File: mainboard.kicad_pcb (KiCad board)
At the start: 2 copper layers, 67.3 x 33.7 mm, 29 parts, among them J1 105017-1001, J2 Conn_01x04_Female, J3 Conn_01x02_Female, J5 Conn_01x02_Female, Q1 AOD4184A, U1 ESP32-WROOM-32E_(16MB), U3 AMS1117-3.3, U4 PAM8403DR

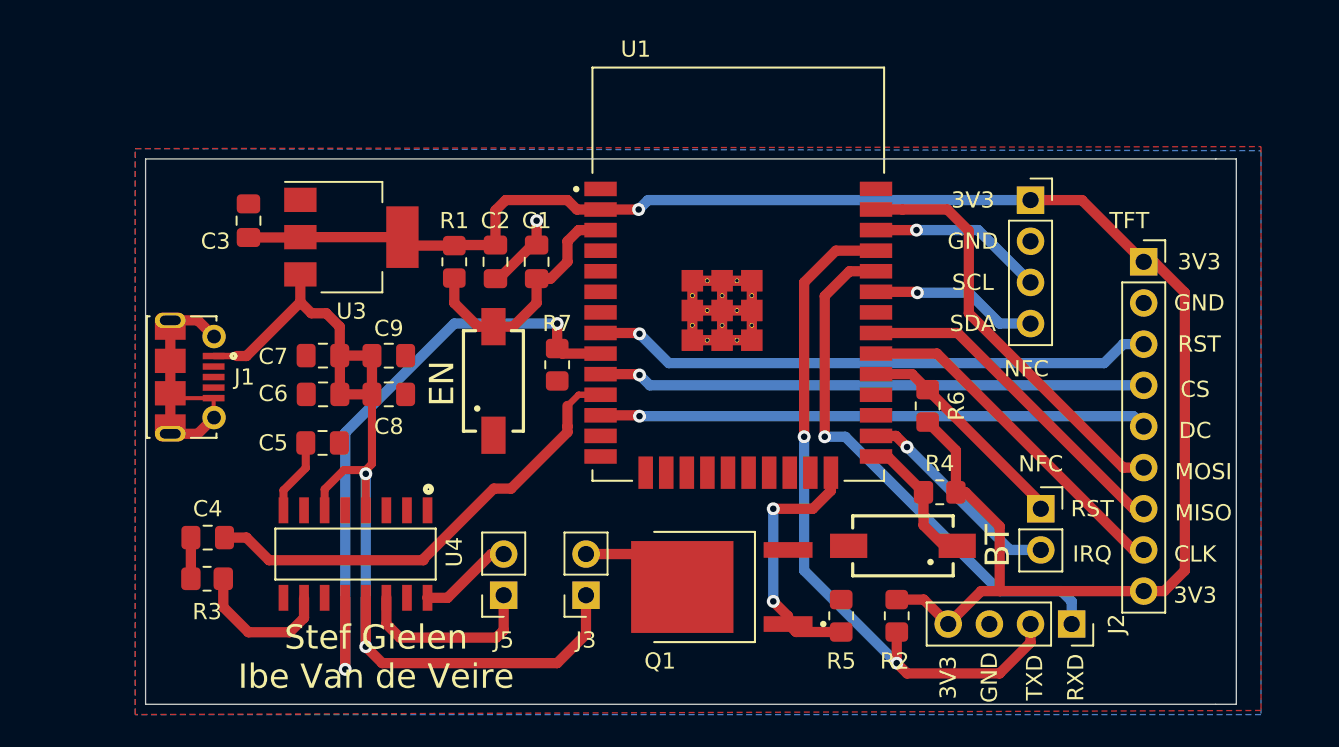
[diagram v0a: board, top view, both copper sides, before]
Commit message: update volgens feedback
blinkled toegevoegd aan io12
paar grondvias toegevoegd
ingangsontkoppeling ldo
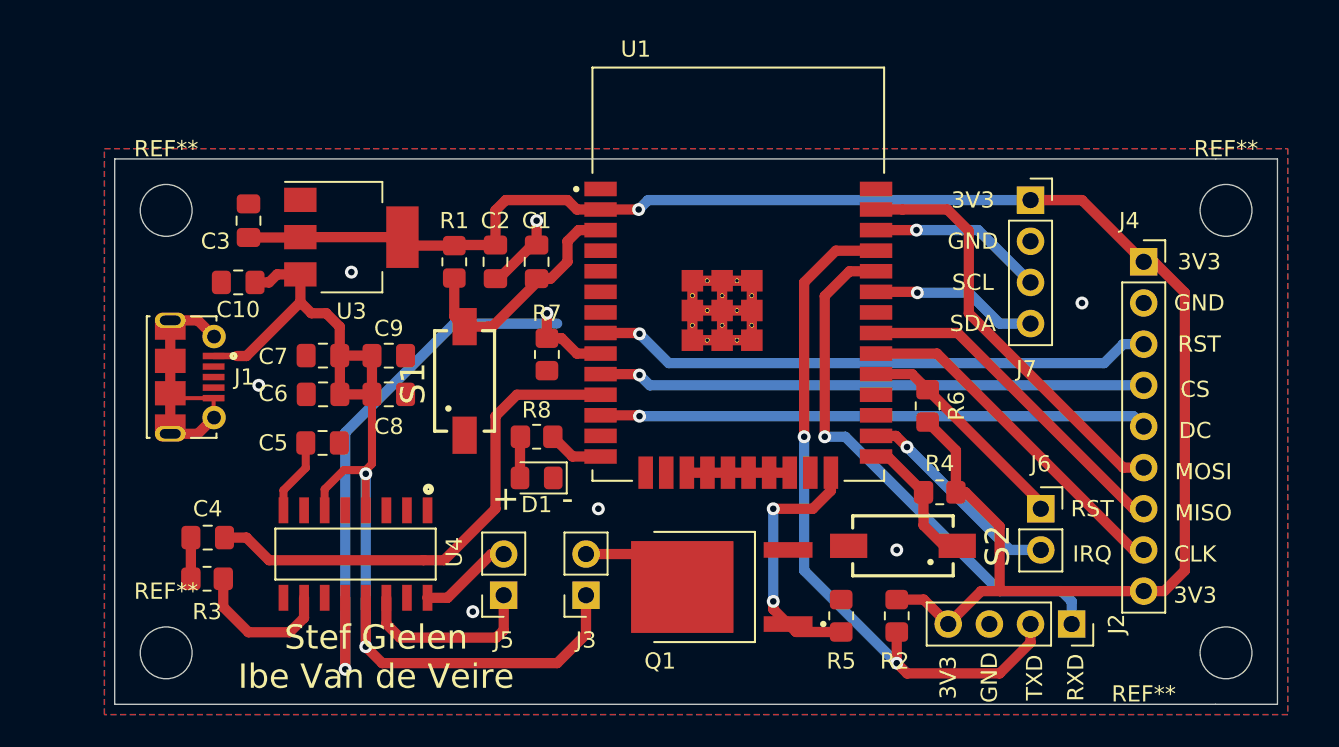
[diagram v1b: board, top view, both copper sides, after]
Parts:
- added C10: 10u, Capacitor_SMD:C_0805_2012Metric_Pad1.18x1.45mm_HandSolder, F.Cu at (83.2, 90.2)
- added D1: LED, LED_SMD:LED_0805_2012Metric_Pad1.15x1.40mm_HandSolder, F.Cu at (101.6, 102.2)
- added R8: 47???, Resistor_SMD:R_0805_2012Metric_Pad1.20x1.40mm_HandSolder, F.Cu at (101.6, 99.7)
- added REF**: MountingHole_3.2mm_M3_DIN965, MountingHole:MountingHole_3.2mm_M3_DIN965, F.Cu at (144.1, 85.7)
- added REF**: MountingHole_3.2mm_M3_DIN965, MountingHole:MountingHole_3.2mm_M3_DIN965, F.Cu at (144.1, 113.0)
- added REF**: MountingHole_3.2mm_M3_DIN965, MountingHole:MountingHole_3.2mm_M3_DIN965, F.Cu at (78.7, 85.7)
- added REF**: MountingHole_3.2mm_M3_DIN965, MountingHole:MountingHole_3.2mm_M3_DIN965, F.Cu at (78.7, 113.0)
- moved S1 1.78 mm to (97.2, 96.3)
- moved R7 0.90 mm to (102.2, 94.6)
- renumbered TFT to J4, NFC to J6, NFC to J7, EN to S1, BT to S2
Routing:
- net Net-(U1-Pad17): track 0.00 -> 6.35 mm
- net Net-(R8-Pad2): track 0.00 -> 3.45 mm
- net 5V: track 64.6 -> 67.9 mm
- net Net-(D1-Pad2): track 0.00 -> 2.55 mm
- net INR: track 29.0 -> 31.4 mm
- net SHND: track 39.2 -> 40.1 mm
- net GND: vias 1 -> 7
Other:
- board size 67.3 x 33.7 mm -> 71.8 x 33.7 mm
- board text added: "+"
- board text added: "-"

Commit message: MAND
elco
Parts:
- added C8: 22u, Capacitor_SMD:CP_Elec_6.3x5.4, F.Cu at (82.5, 88.9)
- C3: value 22u -> 470u; footprint Capacitor_SMD:C_0805_2012Metric_Pad1.18x1.45mm_HandSolder -> Capacitor_SMD:CP_Elec_6.3x5.4
- R8: value 47??? -> TBD
- moved C3 12.8 mm to (82.5, 99.1)
- moved C10 8.64 mm to (76.2, 95.2), turned to 90 degrees
- moved J1 8.54 mm to (73.3, 102.4)
- moved C2 3.86 mm to (98.4, 85.1), turned to 0 degrees
- moved REF** 3.24 mm to (75.6, 86.4)
- moved REF** 3.24 mm to (75.6, 112.4)
- moved R1 2.54 mm to (99.1, 88.9)
- moved U3 1.27 mm to (91.4, 87.4)
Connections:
- C3 pad 1: 3V3 -> 5V
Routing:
- net 5V: track 67.9 -> 83.1 mm
- net GND: track 43.8 -> 40.8 mm
- net Net-(C1-Pad1): track 16.0 -> 14.0 mm
- net 3V3: track 112.9 -> 114.6 mm
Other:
- board size 71.8 x 33.7 mm -> 75.6 x 33.7 mm

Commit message: een paar kleine prutsen aangepast, bijna af denk ik
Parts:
- renumbered S2 to BT, S1 to EN
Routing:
- net GND: track 40.8 -> 42.4 mm

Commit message: autisme dankt u
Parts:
- moved J7 0.63 mm to (132.7, 85.1)
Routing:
- net SDA: track 10.3 -> 11.0 mm
- net SCL: track 10.9 -> 11.5 mm
- net 3V3: track 114.6 -> 114.0 mm

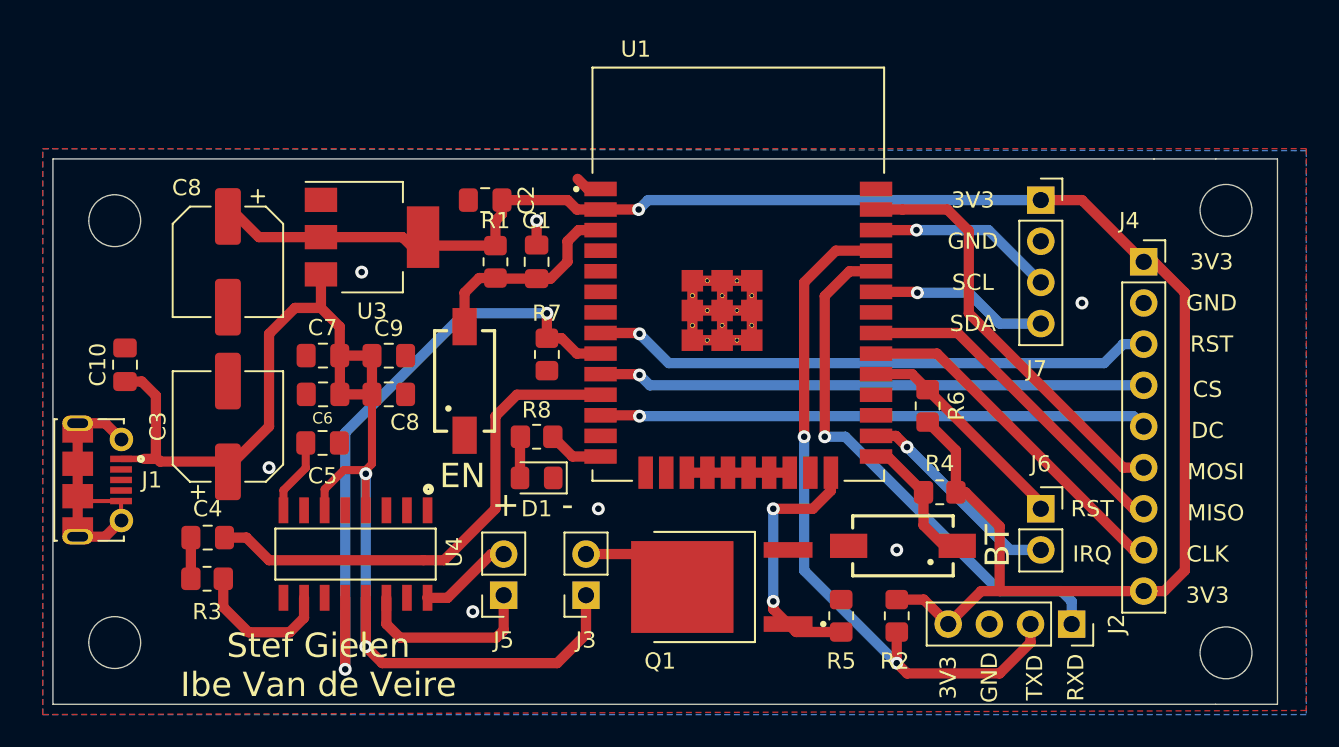
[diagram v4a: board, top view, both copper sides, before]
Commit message: mounting holes juist gezet
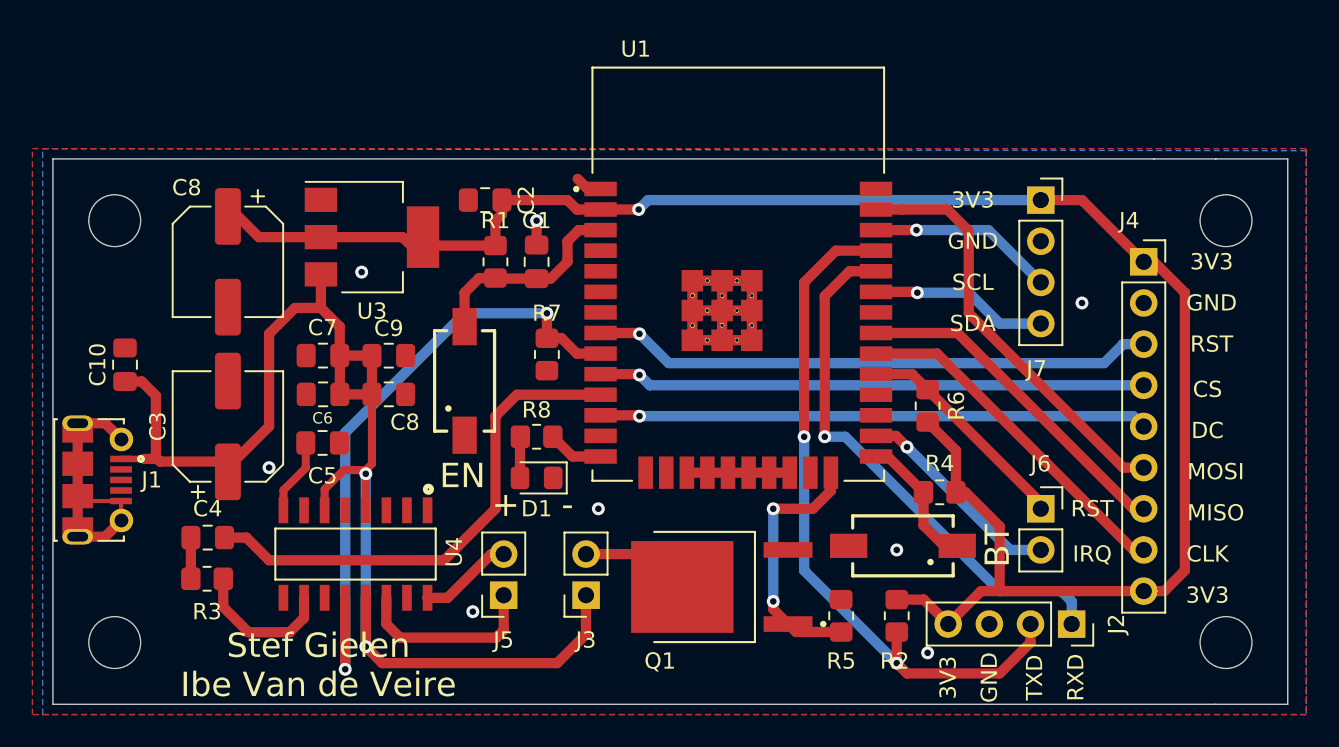
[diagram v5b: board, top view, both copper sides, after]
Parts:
- moved REF** 0.64 mm to (144.1, 86.4)
- moved REF** 0.64 mm to (144.1, 112.4)
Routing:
- net GND: vias 7 -> 8
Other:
- board size 75.6 x 33.7 mm -> 76.2 x 33.7 mm

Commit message: spam github vol
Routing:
- net 5V: track 83.1 -> 77.9 mm, vias 2 -> 0
- net SHND: track 39.8 -> 42.1 mm
- net INR: track 31.4 -> 30.5 mm, vias 0 -> 2

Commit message: Revert "spam github vol"
This reverts commit 94e953e7b075eab7829dab0ec6791751ecd959af.
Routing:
- net 5V: track 77.9 -> 83.1 mm, vias 0 -> 2
- net SHND: track 42.1 -> 39.8 mm
- net INR: track 30.5 -> 31.4 mm, vias 2 -> 0

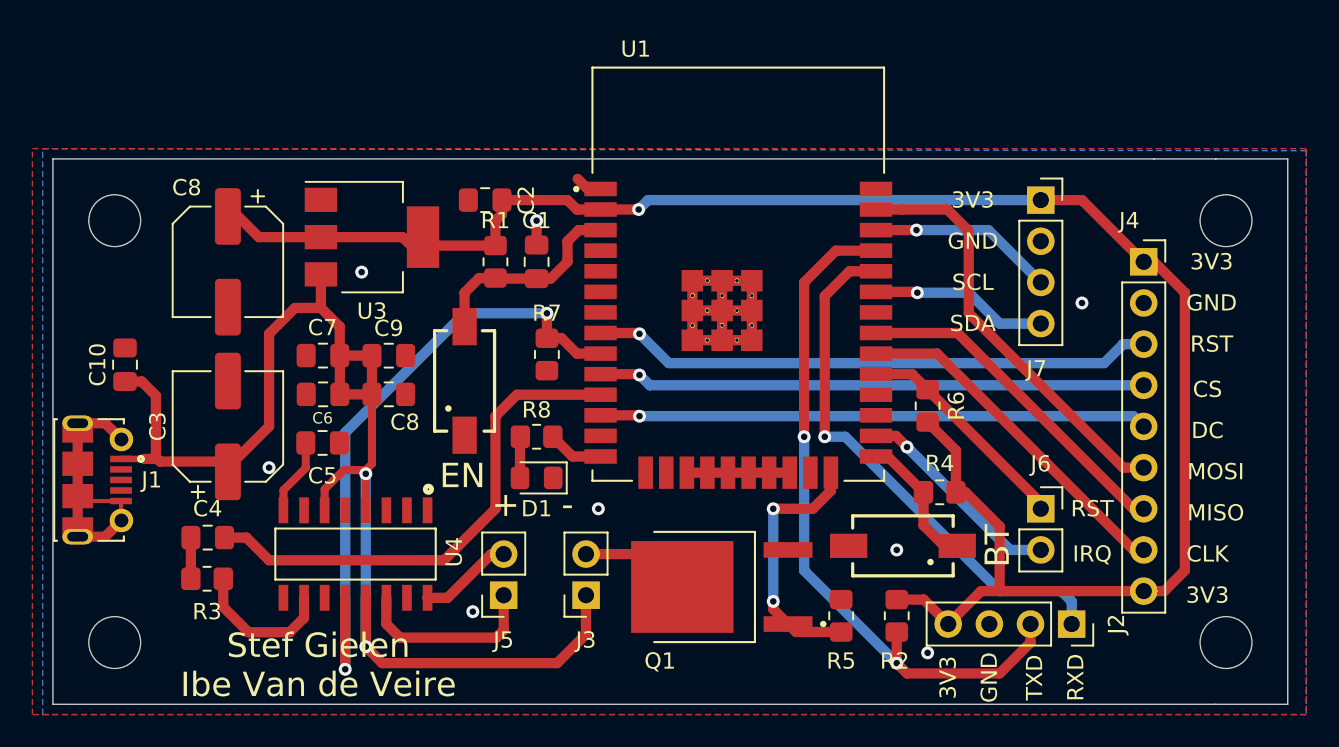
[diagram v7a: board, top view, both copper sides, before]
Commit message: wij waren de ir sensor vergeten, oeps
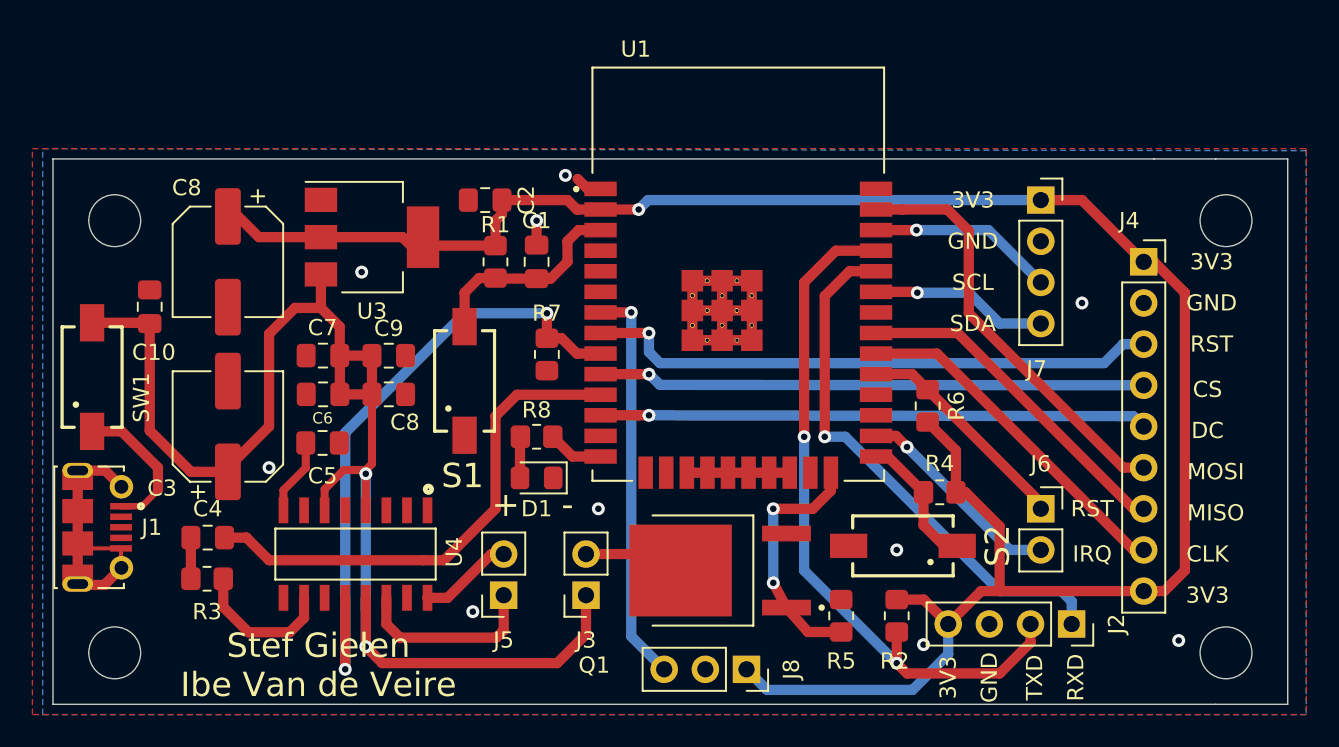
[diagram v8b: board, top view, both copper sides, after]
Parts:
- removed the REF** at (144.1, 112.4)
- removed the REF** at (75.6, 112.4)
- added J8: Conn_01x03_Female, Connector_PinSocket_2.54mm:PinSocket_1x03_P2.54mm_Vertical, F.Cu at (114.6, 114.0)
- added REF**: MountingHole_3.2mm_M3_DIN965, MountingHole:MountingHole_3.2mm_M3_DIN965, F.Cu at (144.1, 113.0)
- added REF**: MountingHole_3.2mm_M3_DIN965, MountingHole:MountingHole_3.2mm_M3_DIN965, F.Cu at (75.6, 113.0)
- added SW1: SW_SPST, 434111043826:434111043826, F.Cu at (74.2, 96.0)
- moved C10 3.89 mm to (77.7, 91.7)
- moved J1 2.92 mm to (73.3, 105.3)
- moved Q1 1.02 mm to (112.9, 108.0)
- renumbered EN to S1, BT to S2
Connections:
- J1 pad 1: 5V -> Net-(J1-Pad1)
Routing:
- net IRB: track 0.00 -> 24.8 mm, vias 0 -> 1
- net 3V3: track 114.0 -> 129.7 mm
- net Net-(J1-Pad1): track 0.00 -> 9.07 mm
- net 5V: track 83.1 -> 86.0 mm
- net TFT_RST: track 35.3 -> 36.0 mm
- net Mosfet_Trig: track 16.1 -> 15.5 mm
- net GND: vias 8 -> 10
